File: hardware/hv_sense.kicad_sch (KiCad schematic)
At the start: 9 parts, among them U1 PC817

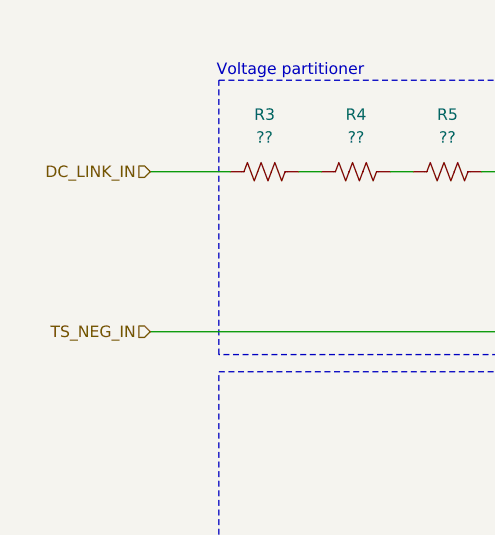
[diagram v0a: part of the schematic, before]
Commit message: add traction system positive input to hv sense block with new dedicated connector
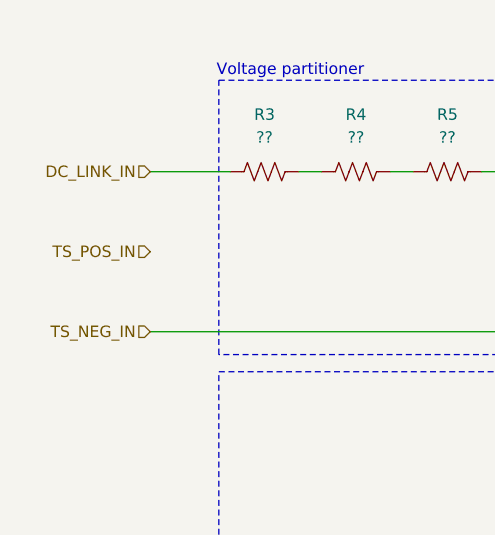
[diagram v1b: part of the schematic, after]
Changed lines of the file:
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@@
+		)
+	)
+	(hierarchical_label "TS_POS_IN"
+		(shape input)
+		(at 35.56 46.99 180)
+		(effects
+			(font
+				(size 1.27 1.27)
+			)
+			(justify right)
 		)
 	)

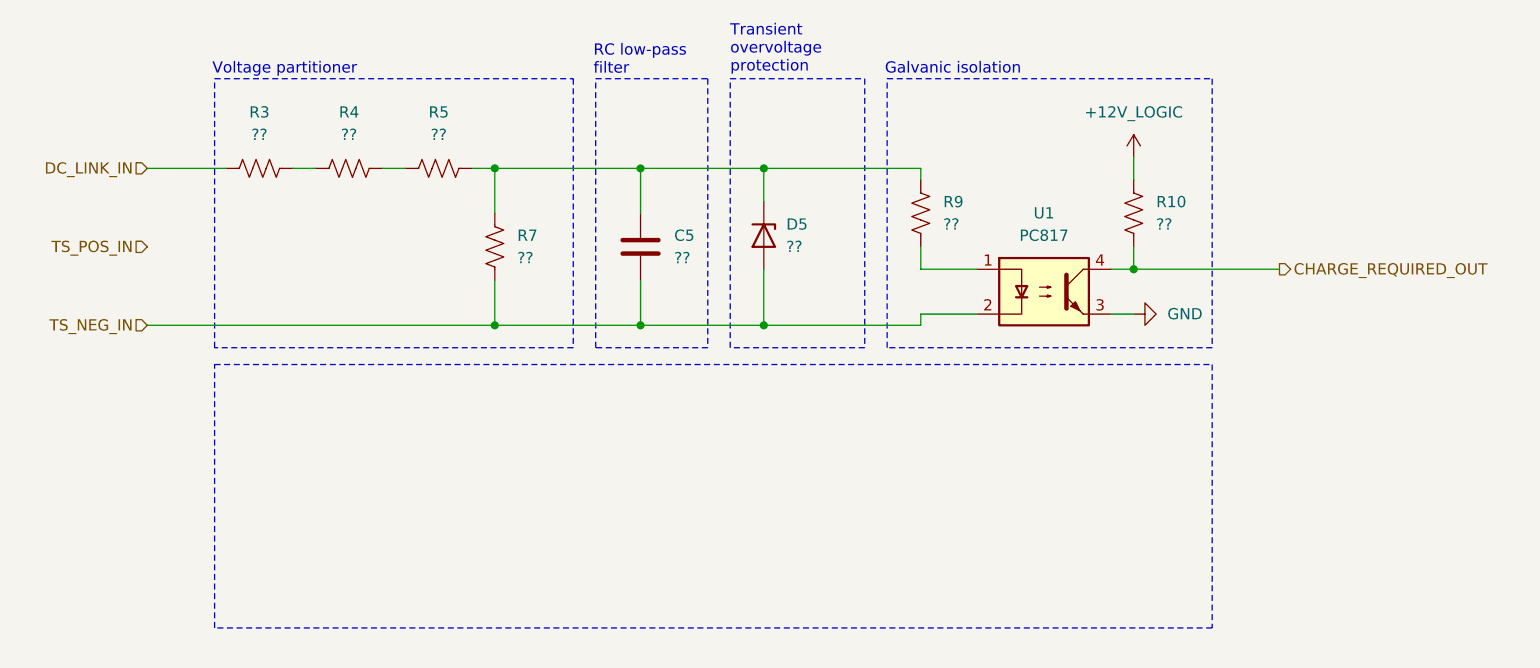
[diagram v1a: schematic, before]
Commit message: refactor project layout merging high and low voltage in the same pcb
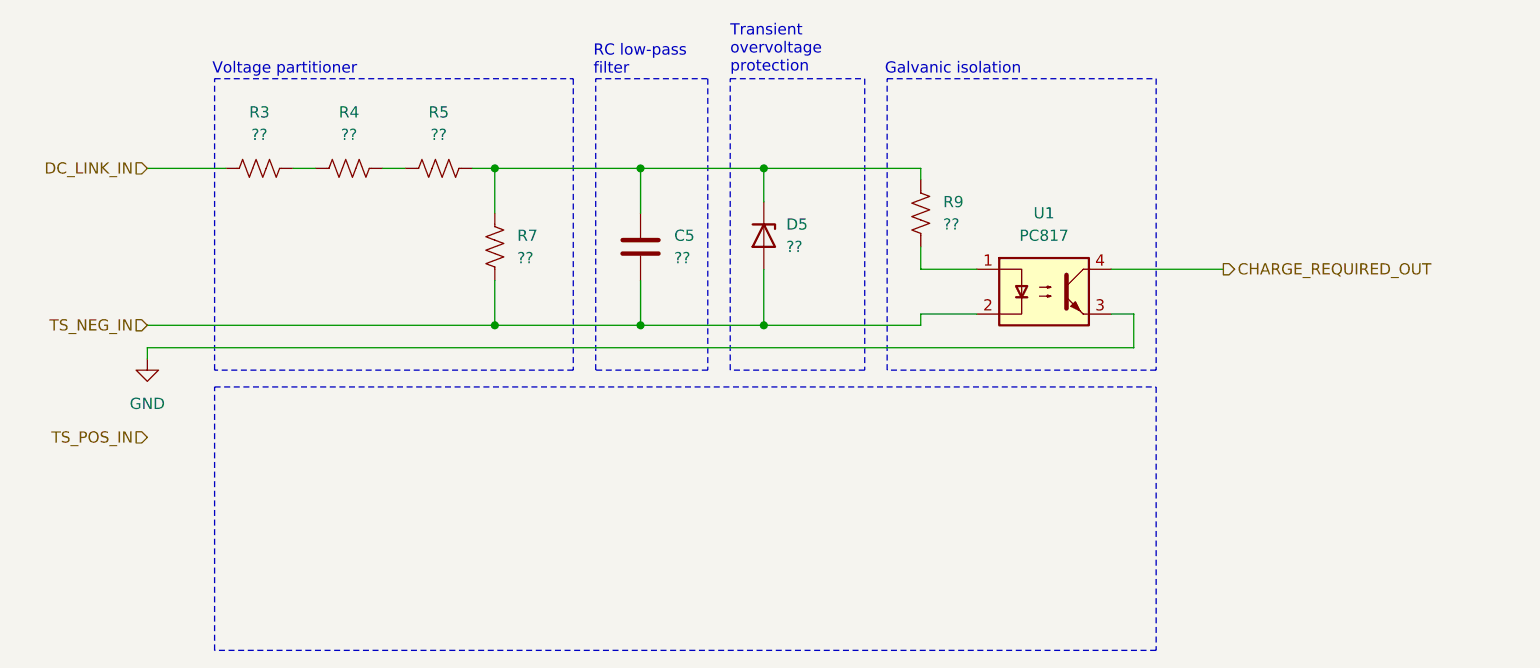
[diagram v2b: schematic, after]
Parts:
- removed R10: ??, symbol Device:R_US
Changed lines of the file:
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@@
 	(rectangle
 		(start 119.38 27.94)
-		(end 156.21 58.42)
+		(end 149.86 60.96)
 		(stroke
 			(width 0)
@@
 	)
 	(rectangle
-		(start 43.18 60.325)
-		(end 156.21 90.17)
+		(start 43.18 62.865)
+		(end 149.86 92.71)
 		(stroke
 			(width 0)
@@
 	(rectangle
 		(start 101.6 27.94)
-		(end 116.84 58.42)
+		(end 116.84 60.96)
 		(stroke
 			(width 0)
@@
 	(rectangle
 		(start 43.18 27.94)
-		(end 83.82 58.42)
+		(end 83.82 60.96)
 		(stroke
 			(width 0)
@@
 	(rectangle
 		(start 86.36 27.94)
-		(end 99.06 58.42)
+		(end 99.06 60.96)
 		(stroke
 			(width 0)
@@
 	)
 	(junction
-		(at 147.32 49.53)
-		(diameter 0)
-		(color 0 0 0 0)
-	)
-	(junction
 		(at 74.93 55.88)
 		(diameter 0)
@@
 	(wire
 		(pts
-			(xy 147.32 36.83) (xy 147.32 39.37)
-		)
-		(stroke
-			(width 0)
-			(type default)
-		)
-	)
-	(wire
-		(pts
-			(xy 147.32 49.53) (xy 163.83 49.53)
+			(xy 144.78 49.53) (xy 157.48 49.53)
 		)
 		(stroke
@@
 	(wire
 		(pts
-			(xy 144.78 49.53) (xy 147.32 49.53)
-		)
-		(stroke
-			(width 0)
-			(type default)
-		)
-	)
-	(wire
-		(pts
 			(xy 91.44 55.88) (xy 105.41 55.88)
 		)
@@
 	(wire
 		(pts
+			(xy 35.56 58.42) (xy 35.56 59.69)
+		)
+		(stroke
+			(width 0)
+			(type default)
+		)
+	)
+	(wire
+		(pts
 			(xy 35.56 38.1) (xy 44.45 38.1)
 		)
@@
 	(wire
 		(pts
-			(xy 147.32 46.99) (xy 147.32 49.53)
-		)
-		(stroke
-			(width 0)
-			(type default)
-		)
-	)
-	(wire
-		(pts
 			(xy 123.19 49.53) (xy 129.54 49.53)
 		)
@@
 		(pts
 			(xy 123.19 54.61) (xy 129.54 54.61)
+		)
+		(stroke
+			(width 0)
+			(type default)
+		)
+	)
+	(wire
+		(pts
+			(xy 35.56 58.42) (xy 147.32 58.42)
+		)
+		(stroke
+			(width 0)
+			(type default)
+		)
+	)
+	(wire
+		(pts
+			(xy 147.32 54.61) (xy 147.32 58.42)
 		)
 		(stroke
@@
 	(hierarchical_label "TS_POS_IN"
 		(shape input)
-		(at 35.56 46.99 180)
+		(at 35.56 68.58 180)
 		(effects
 			(font
@@
 	(hierarchical_label "CHARGE_REQUIRED_OUT"
 		(shape output)
-		(at 163.83 49.53 0)
+		(at 157.48 49.53 0)
 		(effects
 			(font
@@
 			)
 			(justify right)
-		)
-	)
-	(symbol
-		(lib_id "power:GND")
-		(at 147.32 54.61 90)
-		(unit 1)
-		(body_style 1)
-		(exclude_from_sim no)
-		(in_bom yes)
-		(on_board yes)
-		(in_pos_files yes)
-		(dnp no)
-		(fields_autoplaced yes)
-		(property "Reference" "#PWR019"
-			(at 153.67 54.61 0)
-			(hide yes)
-			(show_name no)
-			(do_not_autoplace no)
-			(effects
-				(font
-					(size 1.27 1.27)
-				)
-			)
-		)
-		(property "Value" "GND"
-			(at 151.13 54.6099 90)
-			(show_name no)
-			(do_not_autoplace no)
-			(effects
-				(font
-					(size 1.27 1.27)
-				)
-				(justify right)
-			)
-		)
-		(property "Footprint" ""
-			(at 147.32 54.61 0)
-			(hide yes)
-			(show_name no)
-			(do_not_autoplace no)
-			(effects
-				(font
-					(size 1.27 1.27)
-				)
-			)
-		)
-		(property "Datasheet" ""
-			(at 147.32 54.61 0)
-			(hide yes)
-			(show_name no)
-			(do_not_autoplace no)
-			(effects
-				(font
-					(size 1.27 1.27)
-				)
-			)
-		)
-		(property "Description" "Power symbol creates a global label with name \"GND\" , ground"
-			(at 147.32 54.61 0)
-			(hide yes)
-			(show_name no)
-			(do_not_autoplace no)
-			(effects
-				(font
-					(size 1.27 1.27)
-				)
-			)
-		)
-		(pin "1"
-		)
-		(instances
-			(project "precharge-controller"
-				(path "/d0dc5348-c362-4b06-85a5-76de80ed7055/b60aff46-4517-4be9-addd-53c45289a4c6"
-					(reference "#PWR019")
-					(unit 1)
-				)
-			)
 		)
 	)
@@
 	)
 	(symbol
-		(lib_id "power:+12V")
-		(at 147.32 36.83 0)
-		(unit 1)
-		(body_style 1)
-		(exclude_from_sim no)
-		(in_bom yes)
-		(on_board yes)
-		(in_pos_files yes)
-		(dnp no)
-		(fields_autoplaced yes)
-		(property "Reference" "#PWR018"
-			(at 147.32 40.64 0)
-			(hide yes)
-			(show_name no)
-			(do_not_autoplace no)
-			(effects
-				(font
-					(size 1.27 1.27)
-				)
-			)
-		)
-		(property "Value" "+12V_LOGIC"
-			(at 147.32 31.75 0)
-			(show_name no)
-			(do_not_autoplace no)
-			(effects
-				(font
-					(size 1.27 1.27)
-				)
-			)
-		)
-		(property "Footprint" ""
-			(at 147.32 36.83 0)
-			(hide yes)
-			(show_name no)
-			(do_not_autoplace no)
-			(effects
-				(font
-					(size 1.27 1.27)
-				)
-			)
-		)
-		(property "Datasheet" ""
-			(at 147.32 36.83 0)
-			(hide yes)
-			(show_name no)
-			(do_not_autoplace no)
-			(effects
-				(font
-					(size 1.27 1.27)
-				)
-			)
-		)
-		(property "Description" "Power symbol creates a global label with name \"+12V\""
-			(at 147.32 36.83 0)
-			(hide yes)
-			(show_name no)
-			(do_not_autoplace no)
-			(effects
-				(font
-					(size 1.27 1.27)
-				)
-			)
-		)
-		(pin "1"
-		)
-		(instances
-			(project "precharge-controller"
-				(path "/d0dc5348-c362-4b06-85a5-76de80ed7055/b60aff46-4517-4be9-addd-53c45289a4c6"
-					(reference "#PWR018")
-					(unit 1)
-				)
-			)
-		)
-	)
-	(symbol
 		(lib_id "Device:R_US")
 		(at 123.19 43.18 0)
@@
 	)
 	(symbol
-		(lib_id "Device:R_US")
-		(at 147.32 43.18 0)
+		(lib_id "power:GND")
+		(at 35.56 59.69 0)
 		(unit 1)
 		(body_style 1)
@@
 		(dnp no)
 		(fields_autoplaced yes)
-		(property "Reference" "R10"
-			(at 149.86 41.9099 0)
-			(show_name no)
-			(do_not_autoplace no)
-			(effects
-				(font
-					(size 1.27 1.27)
-				)
-				(justify left)
-			)
-		)
-		(property "Value" "??"
-			(at 149.86 44.4499 0)
-			(show_name no)
-			(do_not_autoplace no)
-			(effects
-				(font
-					(size 1.27 1.27)
-				)
-				(justify left)
+		(property "Reference" "#PWR014"
+			(at 35.56 66.04 0)
+			(hide yes)
+			(show_name no)
+			(do_not_autoplace no)
+			(effects
+				(font
+					(size 1.27 1.27)
+				)
+			)
+		)
+		(property "Value" "GND"
+			(at 35.56 64.77 0)
+			(show_name no)
+			(do_not_autoplace no)
+			(effects
+				(font
+					(size 1.27 1.27)
+				)
 			)
 		)
 		(property "Footprint" ""
-			(at 148.336 43.434 90)
+			(at 35.56 59.69 0)
 			(hide yes)
 			(show_name no)
@@
 		)
 		(property "Datasheet" ""
-			(at 147.32 43.18 0)
-			(hide yes)
-			(show_name no)
-			(do_not_autoplace no)
-			(effects
-				(font
-					(size 1.27 1.27)
-				)
-			)
-		)
-		(property "Description" "Resistor, US symbol"
-			(at 147.32 43.18 0)
+			(at 35.56 59.69 0)
+			(hide yes)
+			(show_name no)
+			(do_not_autoplace no)
+			(effects
+				(font
+					(size 1.27 1.27)
+				)
+			)
+		)
+		(property "Description" "Power symbol creates a global label with name \"GND\" , ground"
+			(at 35.56 59.69 0)
 			(hide yes)
 			(show_name no)
@@
 		)
 		(pin "1"
-		)
-		(pin "2"
 		)
 		(instances
 			(project "precharge-controller"
 				(path "/d0dc5348-c362-4b06-85a5-76de80ed7055/b60aff46-4517-4be9-addd-53c45289a4c6"
-					(reference "R10")
+					(reference "#PWR014")
 					(unit 1)
 				)

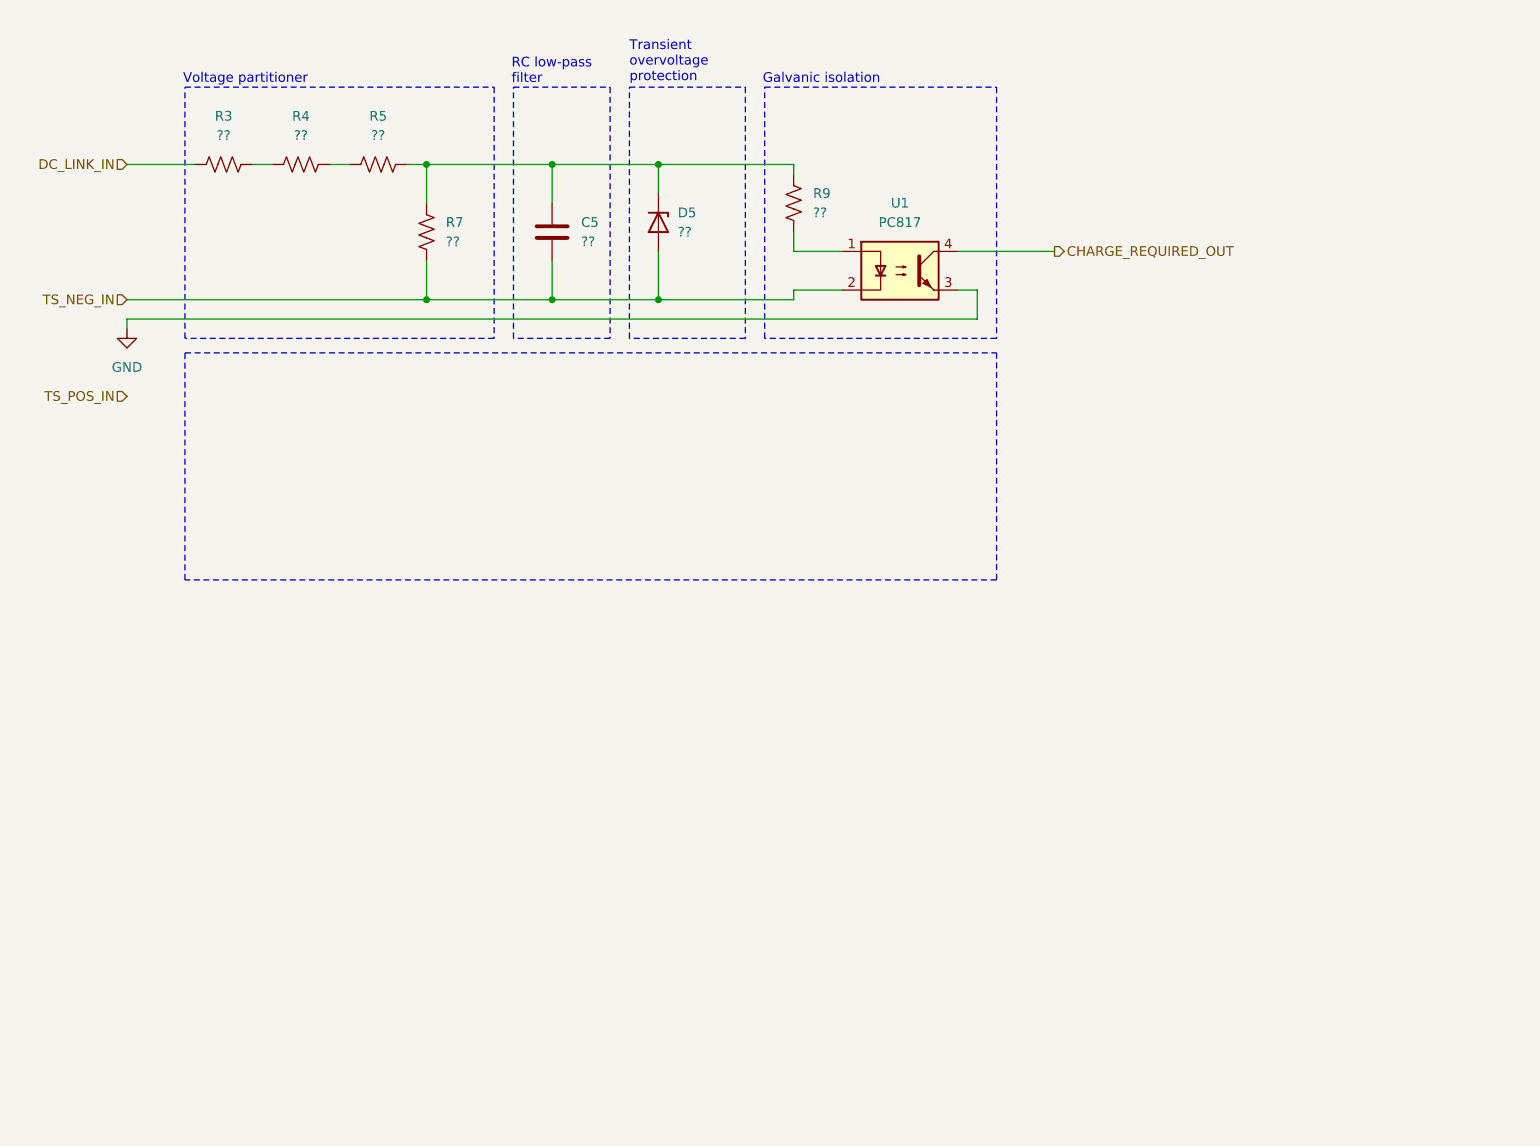
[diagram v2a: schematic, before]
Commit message: add full galvanic isoltation and comparator to hv_sense block
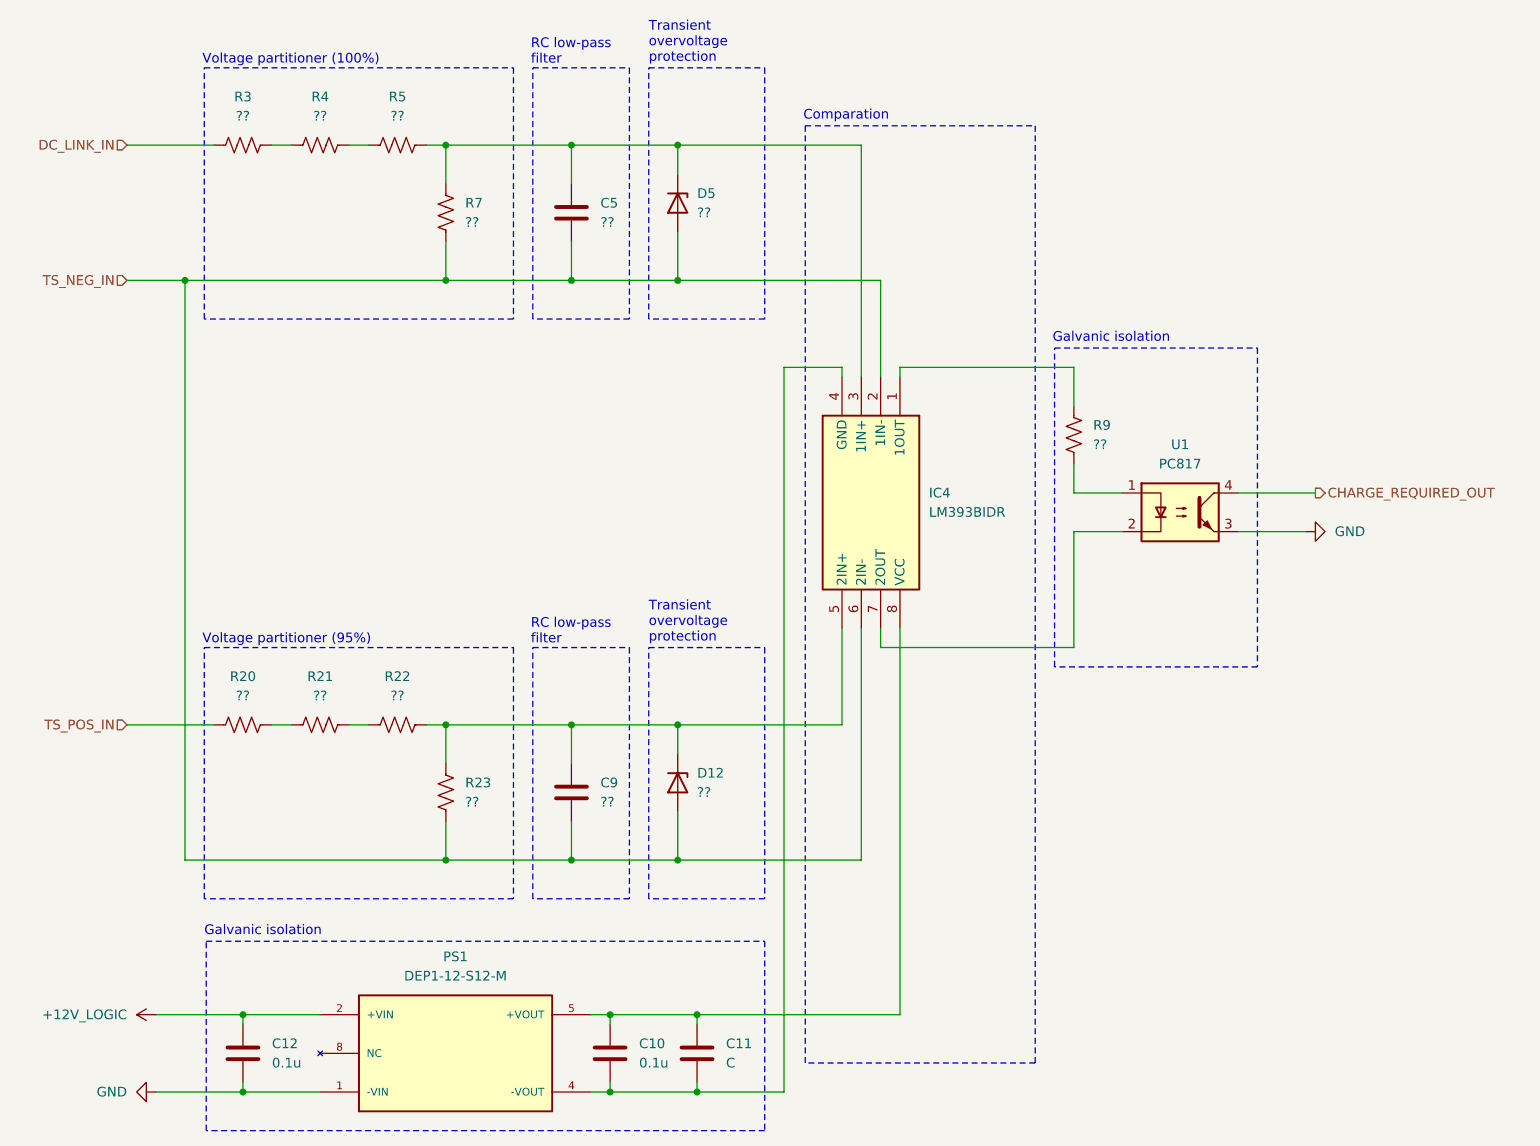
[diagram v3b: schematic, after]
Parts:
- added C10, C12: 0.1u, symbol Device:C
- added C11: C, symbol Device:C
- added C9: ??, symbol Device:C
- added D12: ??, symbol Device:D_Zener
- added IC4: LM393BIDR, SOIC127P600X175-8N, symbol Libary_Loader:LM393BIDR
- added PS1: DEP1-12-S12-M, DEP1-12-S12-M:CONV_DEP1-12-S12-M, symbol DEP1-12-S12-M:DEP1-12-S12-M
- added R20, R21, R22, R23: ??, symbol Device:R_US
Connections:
- net GND: now also C12.2, PS1.1 (-VIN)
- net TS_NEG_IN: now also C9.2, D12.2 (A), IC4.2 (1IN-), IC4.6 (2IN-), R23.1; no longer U1.2
- net TS_POS_IN: now also R20.1
- net at C5.1, D5.1 (K), R5.2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: now also IC4.3 (1IN+); no longer R9.1
- new net: IC4.7 (2OUT), U1.2
- new net: C9.1, D12.1 (K), IC4.5 (2IN+), R22.2, R23.2
- new net: R21.2, R22.1
- new net: R20.2, R21.1
- new net: C10.1, C11.1, IC4.8 (VCC), PS1.5 (+VOUT)
- new net: C10.2, C11.2, IC4.4 (GND), PS1.4 (-VOUT)
- new net: IC4.1 (1OUT), R9.1
- new net +12V_LOGIC: C12.1, PS1.2 (+VIN)
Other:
- note added: "Comparation"
- note added: "Voltage partitioner (100%)"
- note added: "Voltage partitioner (95%)"
- note removed: "Voltage partitioner"
- moved on the sheet: C5, D5, R3, R4, R5, R7, R9, U1

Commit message: refactor schematic and datasheet names
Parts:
- C11: value C -> ??
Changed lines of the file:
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@@
 			)
 		)
-		(property "Value" "C"
+		(property "Value" "??"
 			(at 114.3 156.2099 0)
 			(show_name no)
